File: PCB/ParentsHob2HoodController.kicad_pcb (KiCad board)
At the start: 2 copper layers, 76.8 x 47.2 mm, 43 parts, among them J1 Programming_Header, J2 FromController, J3 ToRelays, J4 Conn_IR, J5 Conn_ExtraFan, J6 Conn_01x02, J7 Conn_01x06, Q1 AO3400A, SW1 SW_SPST, U1 MCP3208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

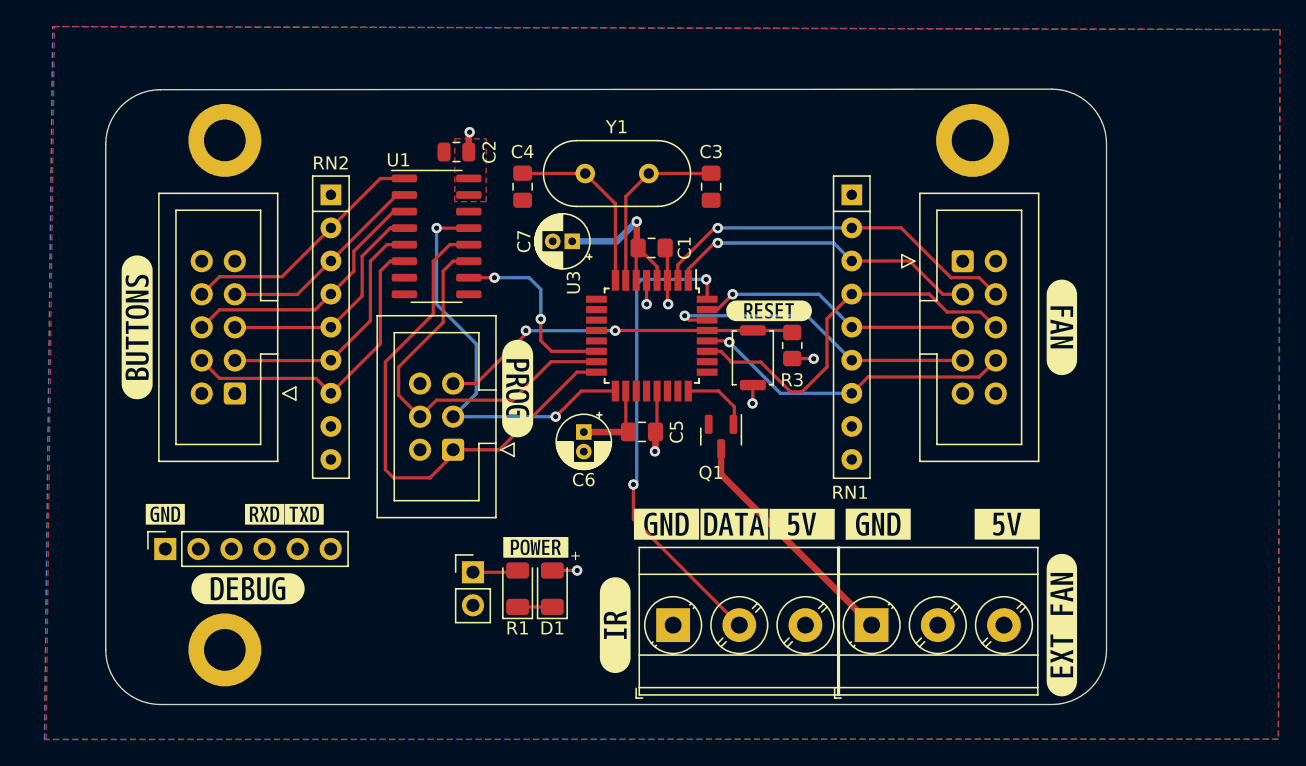
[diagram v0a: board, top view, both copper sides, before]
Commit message: Created base plate to protect solder joins from metal housing on fan.
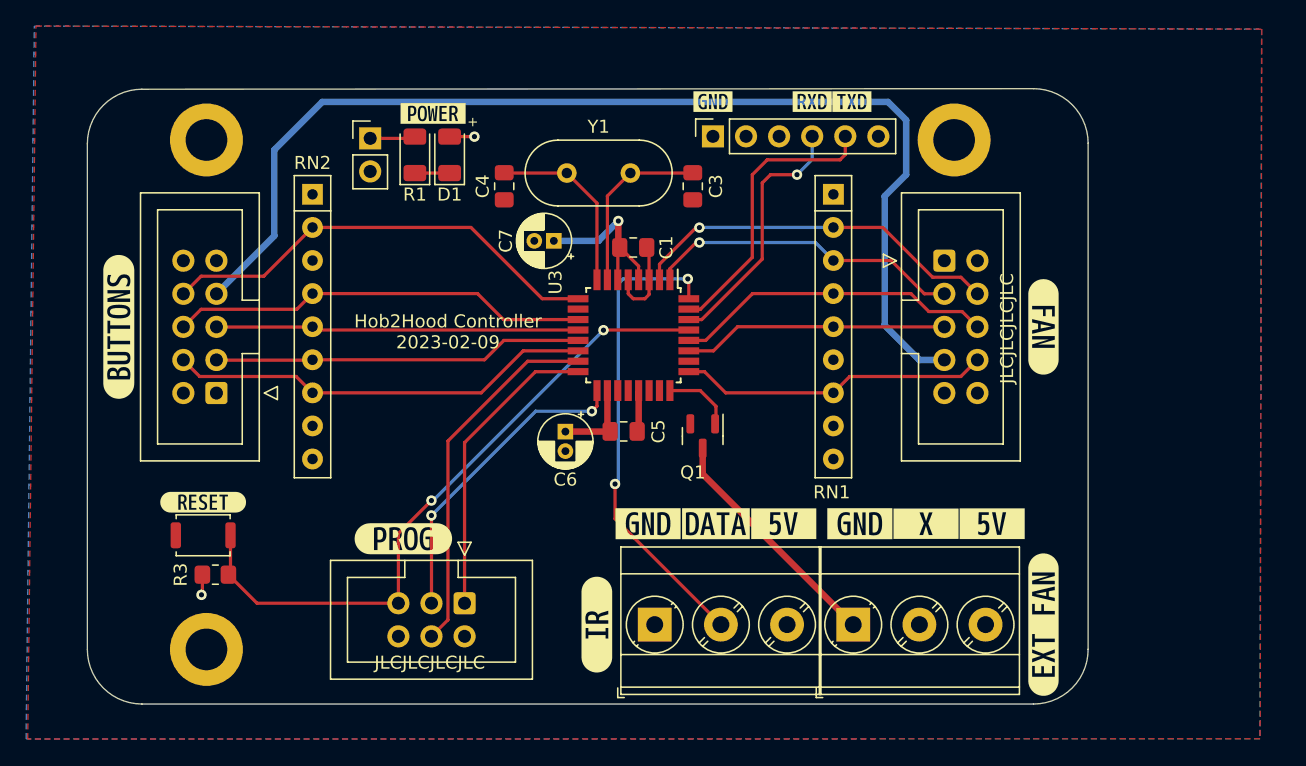
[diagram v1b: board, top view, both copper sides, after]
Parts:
- removed C2: 100nF/16V, Capacitor_SMD:C_0805_2012Metric
- removed U1: MCP3208, Package_SO:SOIC-16_3.9x9.9mm_P1.27mm
- removed kibuzzard-63DE869D: G***, kibuzzard-63DE869D
- added kibuzzard-63E16F65: G***, kibuzzard-63E16F65, F.Cu at (85.8, 51.8)
- moved kibuzzard-63DE866F 52.6 mm to (77.1, 19.4)
- moved kibuzzard-63DE867D 52.6 mm to (80.1, 19.4)
- moved kibuzzard-63DE8685 52.6 mm to (69.5, 19.4)
- moved J7 52.6 mm to (69.5, 22.0)
- moved R3 47.7 mm to (31.3, 55.7), turned to 0 degrees
- moved kibuzzard-63DC4623 45.9 mm to (30.3, 50.1)
- moved SW1 44.4 mm to (30.3, 52.7), turned to 180 degrees
- moved D1 34.2 mm to (49.3, 23.5)
- moved R1 34.2 mm to (46.6, 23.5)
- moved kibuzzard-63DE6880 34.2 mm to (48.0, 20.3)
- moved J6 34.2 mm to (43.2, 22.2)
- moved kibuzzard-63DDA468 14.5 mm to (45.7, 52.9), turned to 0 degrees
- moved J1 11.8 mm to (50.4, 57.9), turned to -90 degrees
- moved kibuzzard-63DDA454 1.41 mm to (94.9, 36.7)
- moved J3 1.41 mm to (87.2, 31.6)
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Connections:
- J2 pad 7: CL_7 -> SPECIAL_7
- J3 pad 7: RL_7 -> SPECIAL_7
- J7 pad 4: S_RX -> RXD
- J7 pad 5: S_TX -> TXD
- RN1 pad 6: RL_7 -> unconnected-(RN1-Pad6)
- RN2 pad 3: CL_7 -> unconnected-(RN2-Pad3)
- U3 pad 10: S_RX -> unconnected-(U3-Pad10)
- U3 pad 11: S_TX -> CL_6
- U3 pad 12: unconnected-(U3-Pad12) -> CL_5
- U3 pad 13: unconnected-(U3-Pad13) -> CL_3
- U3 pad 14: SS -> CL_4
- U3 pad 25: unconnected-(U3-Pad25) -> RL_8
- U3 pad 27: RL_6 -> RL_5
- U3 pad 28: RL_8 -> RL_6
- U3 pad 30: RL_7 -> RXD
- U3 pad 31: RL_5 -> TXD
- U3 pad 9: unconnected-(U3-Pad9) -> CL_8
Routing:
- net SPECIAL_7: track 0.00 -> 85.6 mm
- net RL_7: track 24.6 -> 0.00 mm, vias 1 -> 0
- net RESET: track 28.0 -> 51.2 mm
- net TXD: track 0.00 -> 22.0 mm
- net RXD: track 0.00 -> 19.8 mm, vias 0 -> 1
- net MISO: track 40.8 -> 23.3 mm
- net CL_7: track 16.2 -> 0.00 mm
- net CL_8: track 19.2 -> 34.7 mm
- net SS: track 14.4 -> 0.00 mm, vias 2 -> 0
- net CL_6: track 20.1 -> 32.2 mm
- net CL_5: track 18.0 -> 27.9 mm
- net CL_3: track 19.4 -> 28.4 mm
- net CL_4: track 24.1 -> 32.7 mm
- net SCK: track 32.2 -> 24.1 mm
- net RL_6: track 30.2 -> 24.7 mm
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- removed copper zone on F.Cu, net +5V
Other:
- board text added: "Hob2Hood Controller 2023-02-09"
- board text added: "JLCJLCJLCJLC"
